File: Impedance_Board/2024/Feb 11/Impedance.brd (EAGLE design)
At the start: 70 x 70 mm, 42 parts, among them U2 INA826AID, U4 MC74VHC1GT66DTT1, U7 AD8606ARZ, U8 AD8606ARZ

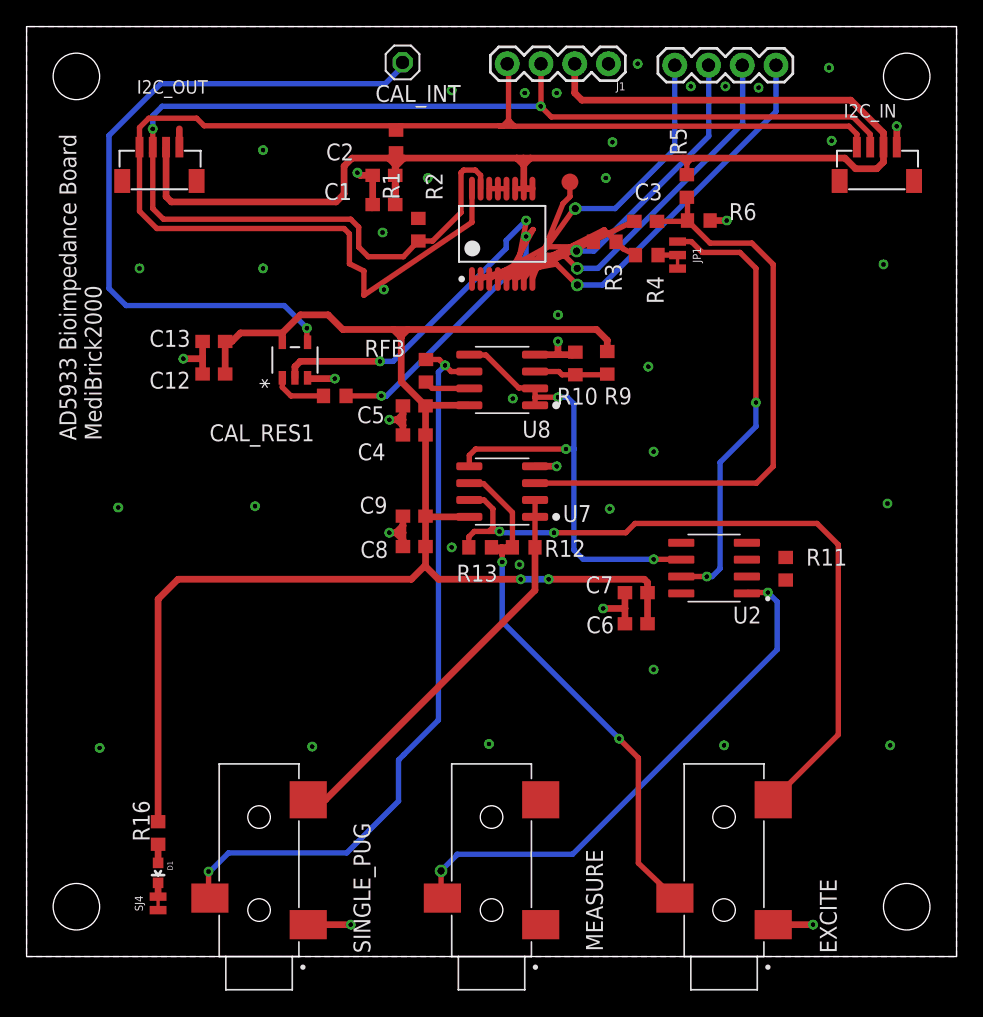
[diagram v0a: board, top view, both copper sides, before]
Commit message: Impedance
Minor change SPO2
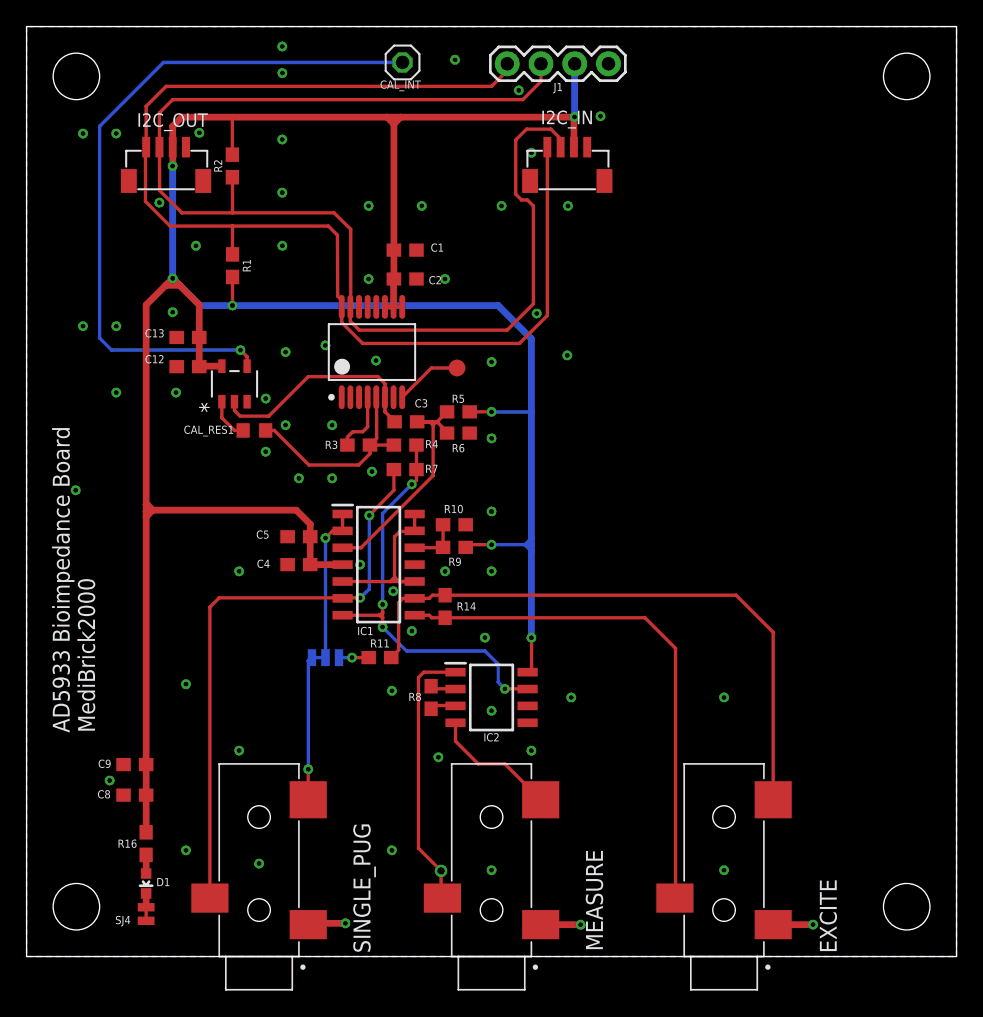
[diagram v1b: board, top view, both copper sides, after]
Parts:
- removed C6: 0.1uF, rcl:C0603
- removed C7: 10uF, rcl:C0603
- removed J5: (no value), SparkFun-Connectors:1X04
- removed R12: 82K, rcl:R0603
- removed R13: 1M, rcl:R0603
- removed RFB: 2K, rcl:R0603
- removed U2: INA826AID, INA826AID:SOIC127P599X175-8N
- removed U7, U8: AD8606ARZ, AD8606ARZ:SOIC127P600X175-8N
- added FRAME1: FRAME-LETTERNO_PACKAGE, SparkFun-Aesthetics:DUMMY
- added IC1: AD8608ARZ, AD8608ARZ:SOIC127P600X175-14N
- added IC2: INA826AID, INA826AID:SOIC127P600X175-8N
- added R14: 1k, SparkFun-Resistors:0603
- added R7: 3.9k, SparkFun-Resistors:0603
- added R8: 5.6k, SparkFun-Resistors:0603
- C3: value 10 nF -> 0.1uF; device rcl:C0603 -> SparkFun-Capacitors:0603
- R1, R2: value 10k -> 4.7k; device rcl:R0603 -> SparkFun-Resistors:0603
- R10: value 20k -> 47k; device rcl:R0603 -> SparkFun-Resistors:0603
- R11: value 1K -> 1k; device rcl:R0603 -> SparkFun-Resistors:0603
- R16: value R__0603 -> 1k; device JLC PCB Basic Parts_loc:R0603 -> SparkFun-Resistors:0603
- R3, R4: device rcl:R0603 -> SparkFun-Resistors:0603
- R5: value 100k -> 47k; device rcl:R0603 -> SparkFun-Resistors:0603
- R6: value 100K -> 47k; device rcl:R0603 -> SparkFun-Resistors:0603
- R9: value 20K -> 47k; device rcl:R0603 -> SparkFun-Resistors:0603
- moved JP1 40.3 mm to (22.5, 22.5), flipped to the bottom, turned to 0 degrees
- moved R11 31.3 mm to (26.6, 22.5), turned to 0 degrees
- moved C8 28.1 mm to (8.15, 12.2)
- moved C9 28.1 mm to (8.15, 14.4)
- moved R5 24.2 mm to (32.5, 41.0), turned to 180 degrees
- moved R6 24.2 mm to (32.5, 39.4)
- moved R3 24.0 mm to (25.0, 38.5)
- moved C3 23.5 mm to (28.6, 40.2)
- moved I2C_IN 23.3 mm to (40.7, 60.0)
- moved R4 23.1 mm to (28.5, 38.5)
- moved R9 18.0 mm to (32.2, 30.8), turned to 0 degrees
- moved TP1 16.4 mm to (32.4, 44.3)
- moved R1 15.5 mm to (15.5, 52.0)
- moved R10 15.2 mm to (32.2, 32.5), turned to 180 degrees
- moved R2 14.8 mm to (15.5, 59.5)
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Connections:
- removed net N$10: AD5933.3, J5.3
- removed net N$11: AD5933.7, J5.4
- removed net N$17: RFB.1, SINGLE_PUG.3, U8.6
- removed net N$3: AD5933.1, J5.1
- removed net N$4: AD5933.2, J5.2
- removed net N$7: RFB.2, U8.7
- new net N$18: IC1.10, IC1.13, IC1.14, IC1.5
- new net N$20: IC2.4, MEASURE.2
- new net N$22: IC2.2, R8.2
- new net N$6: C3.2, IC1.3, R5.2, R6.1
- net 3.3V: now also IC1.4, IC2.8; no longer C6.1, C7.1, U7.8, U8.8
- net GND: now also IC1.11, IC2.5; no longer C6.2, C7.2, U7.4, U8.4
- net N$1: now also IC1.6, R7.1, SINGLE_PUG.3; no longer JP1.2, R4.2
- net N$13: now also IC1.7, IC2.7, R4.2, R7.2; no longer U2.6, U7.5, U8.1, U8.2, U8.5
- net N$14: now also IC1.12; no longer U8.3
- net N$15: now also JP1.3; no longer R12.2, U7.1, U7.2
- net N$19: now also IC1.9, R11.2, R14.1; no longer R13.2, U7.7
- net N$21: now also IC2.1; no longer U2.1
- net N$23: now also IC2.3, R8.1; no longer EXCITE.3, R12.1, R13.1, U7.6
- net N$25: now also EXCITE.3, IC1.8, R14.2; no longer JP1.1, U2.7
- net N$8: now also JP1.1, R11.1; no longer JP1.3
- net N$9: now also IC1.1, IC1.2, JP1.2; no longer C3.2, R5.2, R6.1, U7.3
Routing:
- net N$17: track 56.6 -> 0.00 mm, vias 2 -> 0
- net N$1: track 1.47 -> 44.2 mm, vias 0 -> 2
- net N$23: track 41.6 -> 2.10 mm, vias 2 -> 0
- net N$9: track 45.6 -> 11.8 mm, vias 0 -> 1
- net N$3: track 32.5 -> 0.00 mm, vias 1 -> 0
- net GND: track 40.8 -> 9.08 mm, vias 46 -> 65
- net N$4: track 29.3 -> 0.00 mm, vias 1 -> 0
- net N$10: track 26.2 -> 0.00 mm, vias 1 -> 0
- net N$11: track 22.2 -> 0.00 mm, vias 1 -> 0
- net VOUT: track 37.6 -> 16.8 mm, vias 2 -> 0
- net N$21: track 40.6 -> 20.3 mm, vias 2 -> 1
- net VIN: track 35.7 -> 15.5 mm, vias 2 -> 0
- net N$15: track 30.4 -> 10.8 mm, vias 0 -> 1
- net N$6: track 0.00 -> 18.5 mm
- net 3.3V: track 224.5 -> 207.7 mm, vias 2 -> 7
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
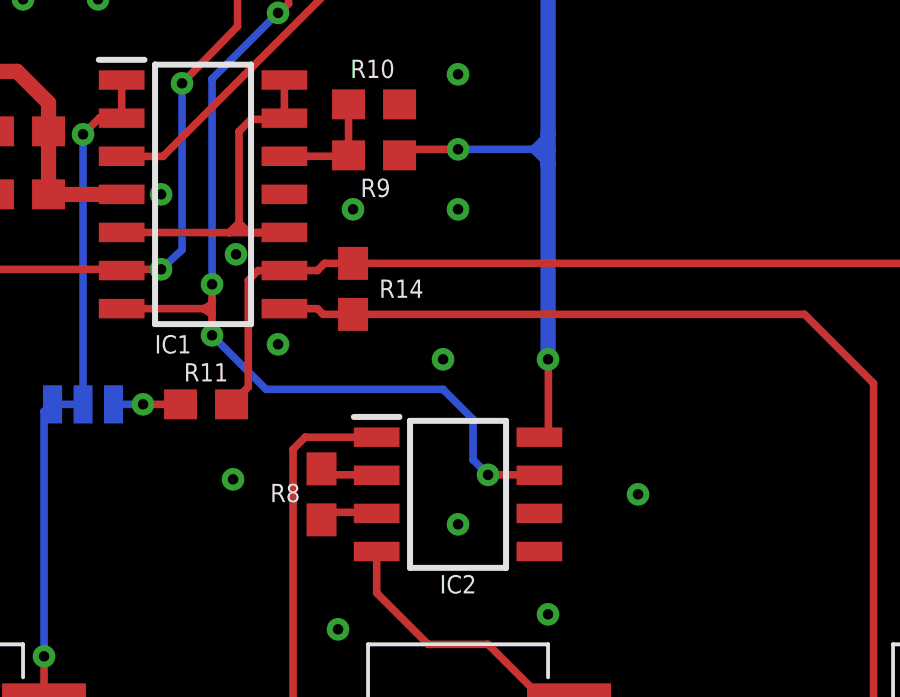
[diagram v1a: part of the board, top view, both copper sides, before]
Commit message: Impedance Vref fic
INA needs Vref
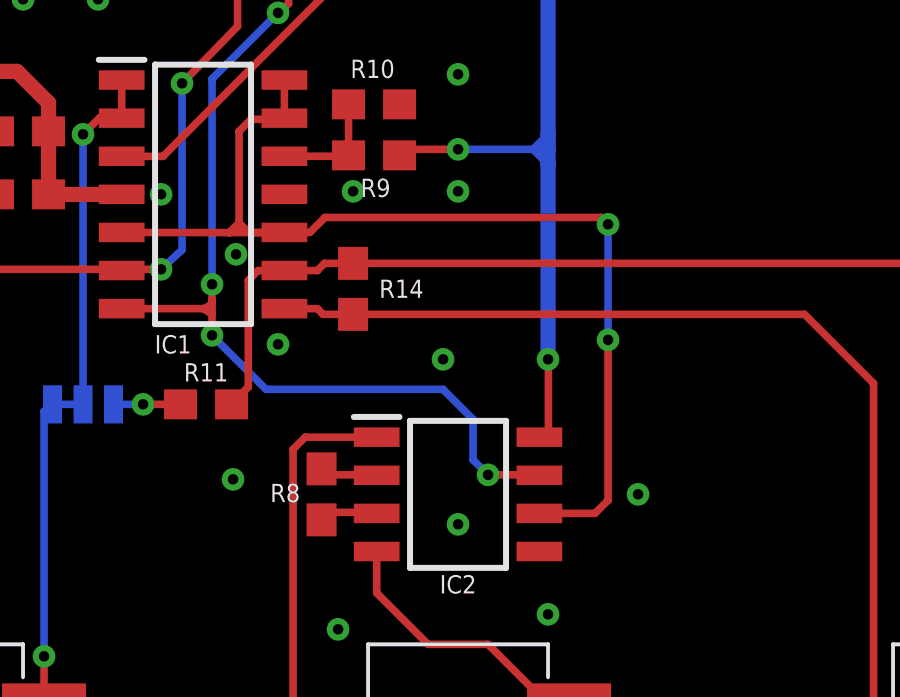
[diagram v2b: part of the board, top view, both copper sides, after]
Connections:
- net N$18: now also IC2.6
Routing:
- net N$18: track 13.5 -> 36.3 mm, vias 0 -> 2
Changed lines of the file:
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@@
 <via x="35" y="39" extent="1-16" drill="0.35"/>
 <via x="35" y="33.5" extent="1-16" drill="0.35"/>
-<via x="35" y="29" extent="1-16" drill="0.35"/>
-<via x="31.5" y="29" extent="1-16" drill="0.35"/>
+<via x="35" y="29.6" extent="1-16" drill="0.35"/>
+<via x="31.5" y="29.6" extent="1-16" drill="0.35"/>
 <via x="29" y="24.5" extent="1-16" drill="0.35"/>
 <via x="34.5" y="24" extent="1-16" drill="0.35"/>
@@
 <wire x1="27.374" y1="28.224" x2="23.788" y2="28.23" width="0.254" layer="1"/>
 <wire x1="27.7" y1="28.55" x2="27.374" y2="28.224" width="0.254" layer="1"/>
+<contactref element="IC2" pad="6"/>
+<wire x1="37.712" y1="18.865" x2="39.565" y2="18.865" width="0.254" layer="1"/>
+<wire x1="39.565" y1="18.865" x2="40" y2="19.3" width="0.254" layer="1"/>
+<wire x1="40" y1="19.3" x2="40" y2="24.65" width="0.254" layer="1"/>
+<via x="40" y="24.65" extent="1-16" drill="0.35"/>
+<wire x1="40" y1="24.65" x2="40" y2="28.5" width="0.254" layer="16"/>
+<via x="40" y="28.5" extent="1-16" drill="0.35"/>
+<wire x1="39.77" y1="28.73" x2="30.562" y2="28.73" width="0.254" layer="1"/>
+<wire x1="30.562" y1="28.73" x2="30.062" y2="28.23" width="0.254" layer="1"/>
+<wire x1="29.212" y1="28.23" x2="30.062" y2="28.23" width="0.254" layer="1"/>
+<wire x1="40" y1="28.5" x2="39.77" y2="28.73" width="0.254" layer="1"/>
 </signal>
 <signal name="N$25">

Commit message: Impedance update
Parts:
- added JP2: JUMPER-SMT_3_1-NC_TRACE_NO-SILK, SparkFun-Jumpers:SMT-JUMPER_3_1-NC_TRACE_NO-SILK
- moved R7 13.6 mm to (20.4, 25.7)
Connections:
- new net N$3: IC1.7, JP2.3, R7.2
- new net N$4: JP2.2, R4.2
- net N$13: now also JP2.1; no longer IC1.7, R4.2, R7.2
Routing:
- net N$13: track 31.8 -> 14.5 mm, vias 4 -> 1
- net N$4: track 0.00 -> 13.8 mm, vias 0 -> 1
- net N$1: track 44.2 -> 35.7 mm, vias 2 -> 1
- net N$3: track 0.00 -> 4.75 mm, vias 0 -> 1
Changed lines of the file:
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@@
 <drawing>
 <settings>
-<setting alwaysvectorfont="no"/>
+<setting alwaysvectorfont="yes"/>
 <setting verticaltext="up"/>
 </settings>
@@
 <attribute name="VALUE" x="35" y="23" size="1.27" layer="27" align="center"/>
 </element>
-<element name="R7" library="SparkFun-Resistors" library_urn="urn:adsk.eagle:library:532" package="0603" package3d_urn="urn:adsk.eagle:package:39650/1" value="3.9k" x="28.5" y="36.65" smashed="yes">
-<attribute name="NAME" x="30.5" y="36.412" size="0.6096" layer="25" font="vector" ratio="20" align="bottom-center"/>
-<attribute name="PROD_ID" value="RES-08701" x="28.5" y="36.65" size="1.778" layer="27" display="off"/>
-<attribute name="VALUE" x="28.5" y="35.888" size="0.6096" layer="27" font="vector" ratio="20" align="top-center"/>
+<element name="R7" library="SparkFun-Resistors" library_urn="urn:adsk.eagle:library:532" package="0603" package3d_urn="urn:adsk.eagle:package:39650/1" value="3.9k" x="20.4" y="25.7" smashed="yes">
+<attribute name="NAME" x="22.4" y="25.462" size="0.6096" layer="25" font="vector" ratio="20" align="bottom-center"/>
+<attribute name="PROD_ID" value="RES-08701" x="20.4" y="25.7" size="1.778" layer="27" display="off"/>
+<attribute name="VALUE" x="20.4" y="24.938" size="0.6096" layer="27" font="vector" ratio="20" align="top-center"/>
 </element>
 <element name="R8" library="SparkFun-Resistors" library_urn="urn:adsk.eagle:library:532" package="0603" package3d_urn="urn:adsk.eagle:package:39650/1" value="5.6k" x="30.45" y="19.5" smashed="yes" rot="R90">
@@
 <attribute name="DESIGNER" value="Nobody" x="-10.7" y="-36.8" size="1.778" layer="27" display="off"/>
 <attribute name="VERSION" value="v01" x="-10.7" y="-36.8" size="1.778" layer="27" display="off"/>
+</element>
+<element name="JP2" library="SparkFun-Jumpers" library_urn="urn:adsk.eagle:library:528" package="SMT-JUMPER_3_1-NC_TRACE_NO-SILK" package3d_urn="urn:adsk.eagle:package:39287/1" value="JUMPER-SMT_3_1-NC_TRACE_NO-SILK" x="27" y="25.65" smashed="yes" rot="MR0">
+<attribute name="NAME" x="27" y="26.793" size="0.6096" layer="26" font="vector" ratio="20" rot="MR0" align="bottom-center"/>
+<attribute name="VALUE" x="27" y="24.507" size="0.6096" layer="28" font="vector" ratio="20" rot="MR0" align="top-center"/>
 </element>
 </elements>
@@
 <via x="35" y="29.6" extent="1-16" drill="0.35"/>
 <via x="31.5" y="29.6" extent="1-16" drill="0.35"/>
-<via x="29" y="24.5" extent="1-16" drill="0.35"/>
-<via x="34.5" y="24" extent="1-16" drill="0.35"/>
+<via x="29.5" y="23" extent="1-16" drill="0.35"/>
+<via x="36.5" y="24" extent="1-16" drill="0.35"/>
 <via x="35" y="18.5" extent="1-16" drill="0.35"/>
 <via x="17.5" y="7" extent="1-16" drill="0.35"/>
@@
 <via x="38" y="60.5" extent="1-16" drill="0.35"/>
 <via x="37.05" y="65.2" extent="1-16" drill="0.35"/>
-<via x="27.6" y="27.5" extent="1-16" drill="0.35"/>
-<via x="25.1" y="29.5" extent="1-16" drill="0.35" diameter="0.55"/>
+<via x="26.25" y="27.25" extent="1-16" drill="0.35"/>
+<via x="26" y="30" extent="1-16" drill="0.35" diameter="0.55"/>
 <via x="10" y="56.75" extent="1-16" drill="0.35"/>
 <via x="38.4" y="48.4" extent="1-16" drill="0.35"/>
@@
 <wire x1="13.8" y1="4.4" x2="13.8" y2="26.3" width="0.254" layer="1"/>
 <wire x1="13.8" y1="26.3" x2="14.5" y2="27" width="0.254" layer="1"/>
-<wire x1="14.5" y1="27" x2="23.738" y2="27" width="0.254" layer="1"/>
+<wire x1="14.5" y1="27" x2="19.2" y2="27" width="0.254" layer="1"/>
+<wire x1="19.2" y1="27" x2="19.5" y2="27" width="0.254" layer="1"/>
+<wire x1="19.5" y1="27" x2="19.8" y2="27" width="0.254" layer="1"/>
+<wire x1="19.8" y1="27" x2="23.738" y2="27" width="0.254" layer="1"/>
 <wire x1="23.738" y1="27" x2="23.788" y2="26.96" width="0.254" layer="1"/>
 <wire x1="23.788" y1="26.96" x2="23.828" y2="27" width="0.254" layer="1"/>
 <wire x1="23.828" y1="27" x2="25.1" y2="27" width="0.254" layer="1"/>
 <via x="25.1" y="27" extent="1-16" drill="0.35"/>
-<wire x1="25.1" y1="27" x2="25.8" y2="27.65" width="0.254" layer="16"/>
-<wire x1="25.8" y1="33.2" x2="25.8" y2="27.65" width="0.254" layer="16"/>
-<via x="25.8" y="33.2" extent="1-16" drill="0.35"/>
-<wire x1="27.65" y1="36.65" x2="27.65" y2="35.1" width="0.254" layer="1"/>
-<wire x1="27.65" y1="35.1" x2="25.8" y2="33.2" width="0.254" layer="1"/>
+<wire x1="19.55" y1="25.7" x2="19.5" y2="25.75" width="0.254" layer="1"/>
+<wire x1="19.5" y1="25.75" x2="19.5" y2="26.7" width="0.254" layer="1"/>
+<wire x1="19.5" y1="27" x2="19.5" y2="26.7" width="0.254" layer="1"/>
+<wire x1="19.5" y1="26.7" x2="19.8" y2="27" width="0.254" layer="1"/>
+<wire x1="19.5" y1="26.7" x2="19.2" y2="27" width="0.254" layer="1"/>
 </signal>
 <signal name="N$22">
@@
 </signal>
 <signal name="N$13">
-<contactref element="R7" pad="2"/>
-<contactref element="IC1" pad="7"/>
-<contactref element="R4" pad="2"/>
 <contactref element="IC2" pad="7"/>
-<wire x1="26.54" y1="25.69" x2="26.51" y2="25.69" width="0.254" layer="1"/>
-<via x="26.8" y="26.5" extent="1-16" drill="0.35"/>
-<wire x1="26.51" y1="25.69" x2="23.788" y2="25.69" width="0.254" layer="1"/>
-<wire x1="26.8" y1="26.5" x2="26.8" y2="33.347871875" width="0.254" layer="16"/>
-<wire x1="29" y1="35.55" x2="26.8" y2="33.347871875" width="0.254" layer="16"/>
-<via x="29" y="35.55" extent="1-16" drill="0.35"/>
-<wire x1="29.35" y1="36.65" x2="29.35" y2="38.5" width="0.254" layer="1"/>
-<wire x1="29" y1="35.55" x2="29.35" y2="35.85" width="0.254" layer="1"/>
-<wire x1="29.35" y1="35.85" x2="29.35" y2="36.65" width="0.254" layer="1"/>
-<via x="26.8" y="24.8" extent="1-16" drill="0.35"/>
-<wire x1="26.8" y1="24.8" x2="28.6" y2="23" width="0.254" layer="16"/>
-<wire x1="28.6" y1="23" x2="34.5" y2="23" width="0.254" layer="16"/>
-<wire x1="34.5" y1="23" x2="35.5" y2="22" width="0.254" layer="16"/>
-<wire x1="35.5" y1="22" x2="35.5" y2="20.65" width="0.254" layer="16"/>
+<wire x1="35.5" y1="25" x2="35.5" y2="20.65" width="0.254" layer="16"/>
 <wire x1="35.5" y1="20.65" x2="36" y2="20.15" width="0.254" layer="16"/>
 <via x="36" y="20.15" extent="1-16" drill="0.35"/>
 <wire x1="36" y1="20.15" x2="37.697" y2="20.15" width="0.254" layer="1"/>
 <wire x1="37.697" y1="20.15" x2="37.712" y2="20.135" width="0.254" layer="1"/>
-<wire x1="26.8" y1="24.8" x2="26.8" y2="25.5" width="0.254" layer="1"/>
-<wire x1="26.8" y1="25.5" x2="26.8" y2="25.85" width="0.254" layer="1"/>
-<wire x1="26.8" y1="25.95" x2="26.8" y2="26.5" width="0.254" layer="1"/>
-<wire x1="26.8" y1="25.95" x2="26.8" y2="25.85" width="0.254" layer="1"/>
-<wire x1="26.8" y1="25.85" x2="26.54" y2="25.69" width="0.254" layer="1"/>
-<wire x1="26.51" y1="25.69" x2="26.8" y2="25.5" width="0.254" layer="1"/>
+<contactref element="JP2" pad="1"/>
+<wire x1="28.016" y1="25.65" x2="34.85" y2="25.65" width="0.254" layer="16"/>
+<wire x1="35.5" y1="25" x2="34.85" y2="25.65" width="0.254" layer="16"/>
+</signal>
+<signal name="N$3">
+<contactref element="R7" pad="2"/>
+<contactref element="IC1" pad="7"/>
+<contactref element="JP2" pad="3"/>
+<wire x1="23.788" y1="25.69" x2="21.26" y2="25.69" width="0.254" layer="1"/>
+<wire x1="21.26" y1="25.69" x2="21.25" y2="25.7" width="0.254" layer="1"/>
+<via x="25.1" y="25.65" extent="1-16" drill="0.35"/>
+<wire x1="25.984" y1="25.65" x2="25.1" y2="25.65" width="0.254" layer="16"/>
+<wire x1="25.1" y1="25.65" x2="23.828" y2="25.65" width="0.254" layer="1"/>
+<wire x1="23.828" y1="25.65" x2="23.788" y2="25.69" width="0.254" layer="1"/>
+</signal>
+<signal name="N$4">
+<contactref element="R4" pad="2"/>
+<contactref element="JP2" pad="2"/>
+<wire x1="29.35" y1="38.5" x2="29.35" y2="37.05" width="0.254" layer="1"/>
+<via x="29.35" y="37.05" extent="1-16" drill="0.35"/>
+<wire x1="27" y1="34.7" x2="27" y2="25.65" width="0.254" layer="16"/>
+<wire x1="27" y1="34.7" x2="29.35" y2="37.05" width="0.254" layer="16"/>
 </signal>
 </signals>
